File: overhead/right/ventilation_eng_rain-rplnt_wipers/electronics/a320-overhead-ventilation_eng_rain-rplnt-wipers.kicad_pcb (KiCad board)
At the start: 2 copper layers, 145 x 170.2 mm, 71 parts, among them J1 Conn_02x01, J2 Conn_02x20_Counter_Clockwise, J3 Conn_02x01, J4 Conn_02x02_Counter_Clockwise

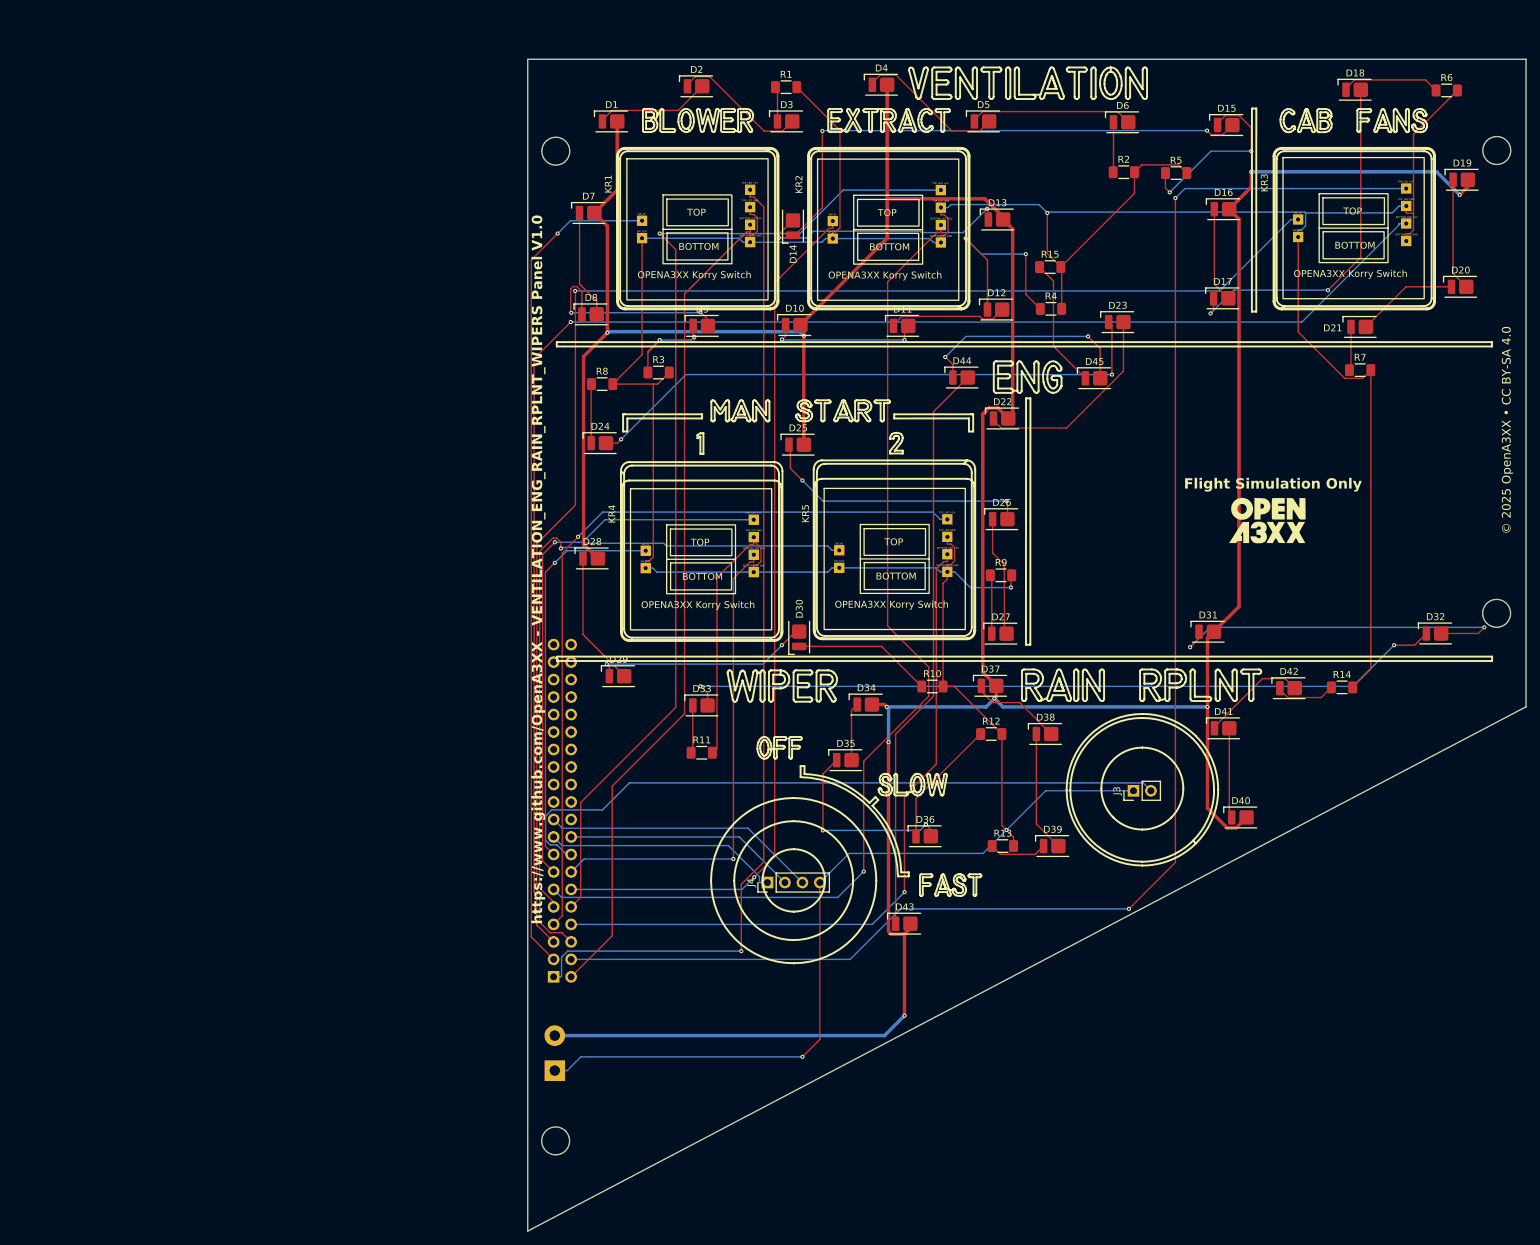
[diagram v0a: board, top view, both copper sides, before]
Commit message: Ventilation Eng Rain Replt and Wipers PCB Changes
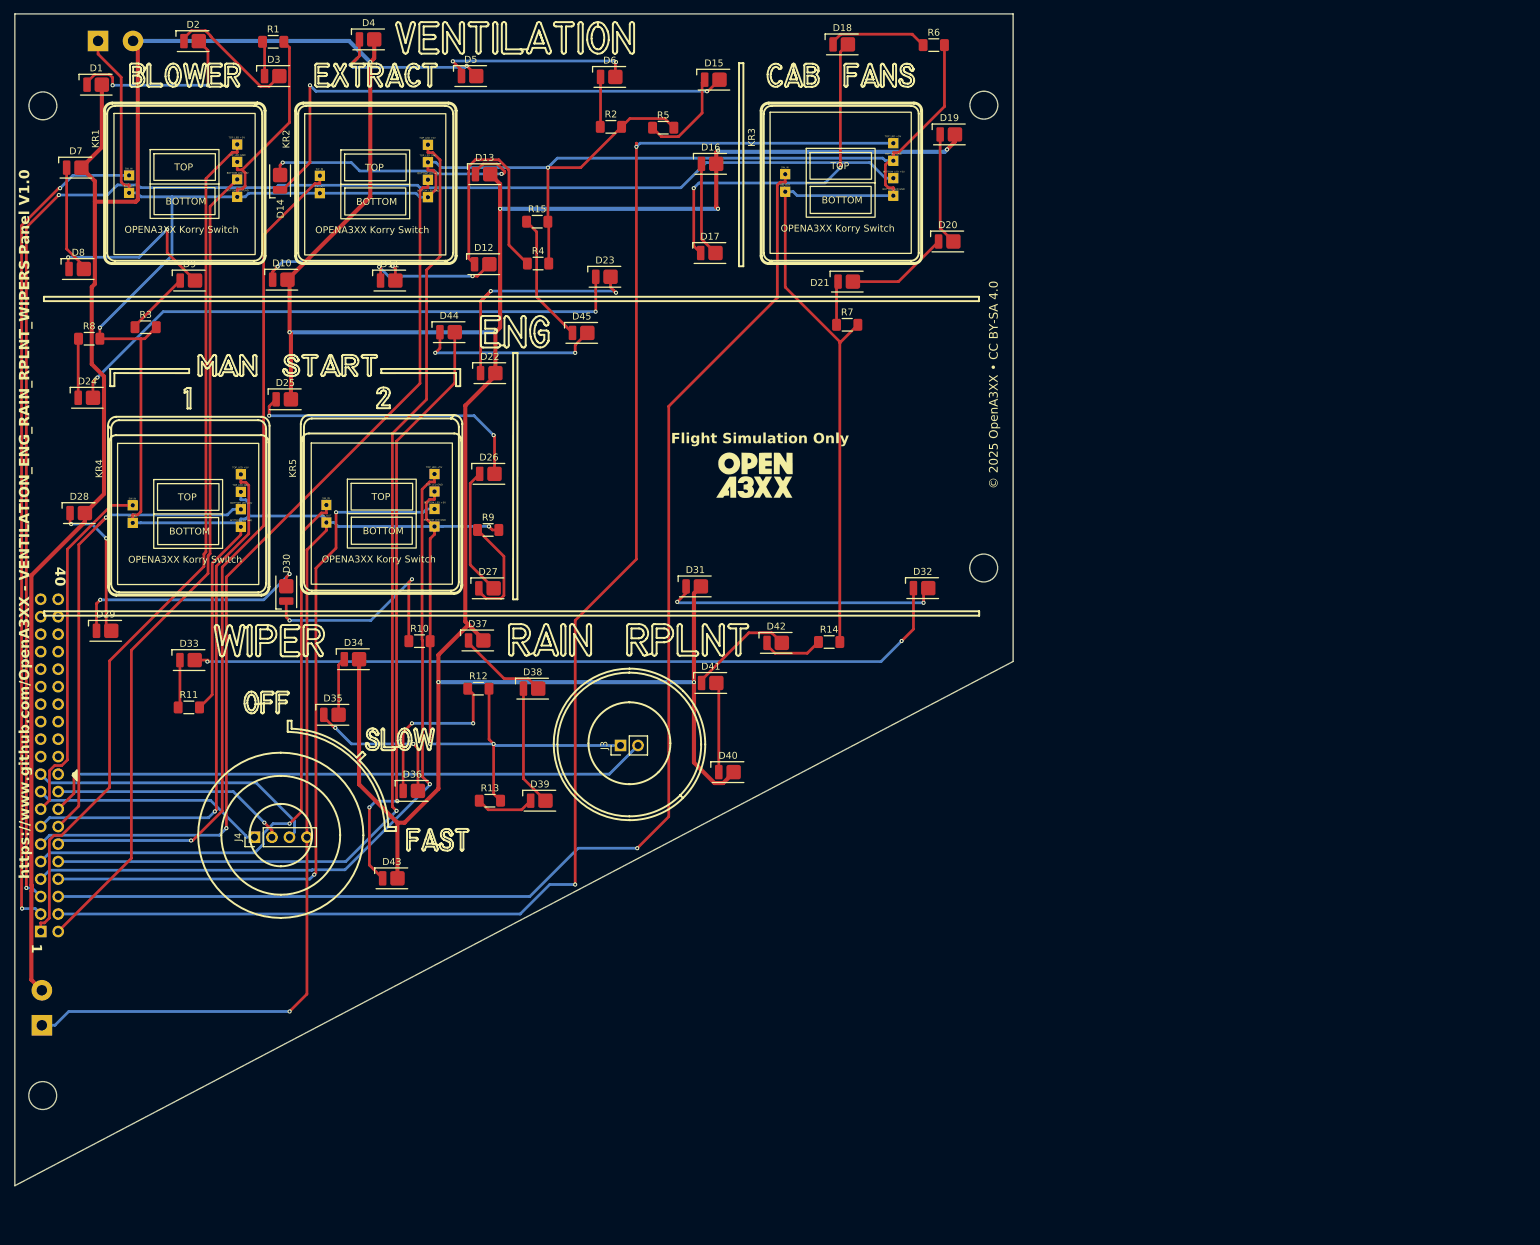
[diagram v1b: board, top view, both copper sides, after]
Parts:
- added J5: Conn_02x01, TerminalBlock:TerminalBlock_bornier-2_P5.08mm, B.Cu at (31.6, 21.1)
- moved D1 75.1 mm to (31.3, 27.5)
- moved D12 74.8 mm to (87.6, 53.6)
- moved D13 74.8 mm to (87.7, 40.5)
- moved D22 74.8 mm to (88.5, 69.4)
- moved D26 74.8 mm to (88.4, 84.0)
- moved D27 74.8 mm to (88.2, 100.6)
- moved D30 74.8 mm to (58.9, 101.1)
- moved D36 74.8 mm to (77.2, 130.1)
- moved D37 74.8 mm to (86.7, 108.2)
- moved KR5 74.8 mm to (62.5, 79.5)
- moved R5 74.8 mm to (113.7, 33.7)
- moved D10 74.8 mm to (58.3, 55.8)
- moved D11 74.8 mm to (74.0, 55.9)
- moved D14 74.8 mm to (58.0, 41.4)
- moved D16 74.8 mm to (120.6, 39.0)
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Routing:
- net GND: track 621.1 -> 668.7 mm, vias 4 -> 6
- net +12V: track 538.3 -> 579.1 mm
- net Net-(J2-Pin_11): track 150.9 -> 134.7 mm
- net Net-(J2-Pin_1): track 143.5 -> 127.5 mm, vias 1 -> 0
- net Net-(J2-Pin_6): track 209.2 -> 194.2 mm
- net Net-(D9-K): track 23.9 -> 9.50 mm, vias 2 -> 0
- net Net-(D15-K): track 27.1 -> 14.1 mm, vias 2 -> 0
- net Net-(D22-K): track 30.1 -> 43.1 mm, vias 0 -> 2
- net Net-(D31-K): track 53.3 -> 41.0 mm
- net Net-(D30-K): track 20.2 -> 32.4 mm, vias 0 -> 2
- net Net-(J2-Pin_9): track 98.7 -> 88.3 mm
- net Net-(D1-K): track 16.7 -> 26.7 mm, vias 0 -> 2
- net Net-(J2-Pin_5): track 221.0 -> 229.9 mm, vias 1 -> 2
- net Net-(J2-Pin_16): track 98.5 -> 89.7 mm, vias 0 -> 1
- net Net-(D4-K): track 21.6 -> 29.7 mm, vias 0 -> 2
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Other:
- board text added: "+12V Variable Backlight"
- board text added: "1"
- board text added: "40"
- board text added: "GND"
- board text added: "[CONNECTION J2] 1-BLOWER-TOP_LED 2-BLOWER-BOTTOM_LED 3-BLOWER-KORRY_SW 4-CAB-FANS-TOP_LED 5-CAB-FANS-BOTTOM_LED 6-CAB-FANS-KORRY_SW 7-MAN-START-ENG-2-TOP_LED 8-MAN-START-ENG-2-BOTTOM_LED 9-MAN-START-ENG-2-KORRY_SW 10-EXTRACT-TOP_LED 11-EXTRACT-BOTTOM_LED 12-EXTRACT-KORRY_SW 13-MAN-START-ENG-1-TOP_LED 14-MAN-START-ENG-1-BOTTOM_LED 15-MAN-START-ENG-1-KORRY_SW 16-RAIN-RPLNT-SW 17-WIPER-SW-POS-1 18-W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"
